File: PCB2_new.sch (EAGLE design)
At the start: 103 parts

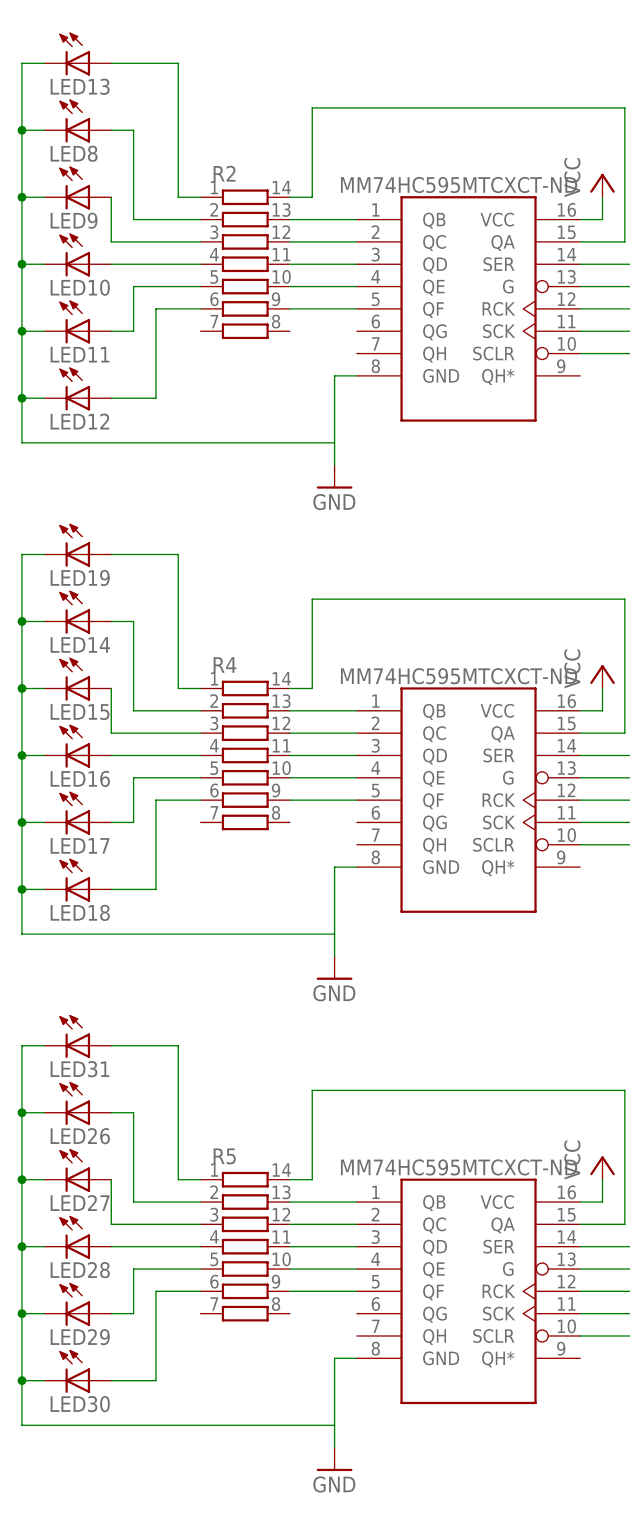
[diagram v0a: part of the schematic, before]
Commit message: Added ESD protection resistors on PCB1_new
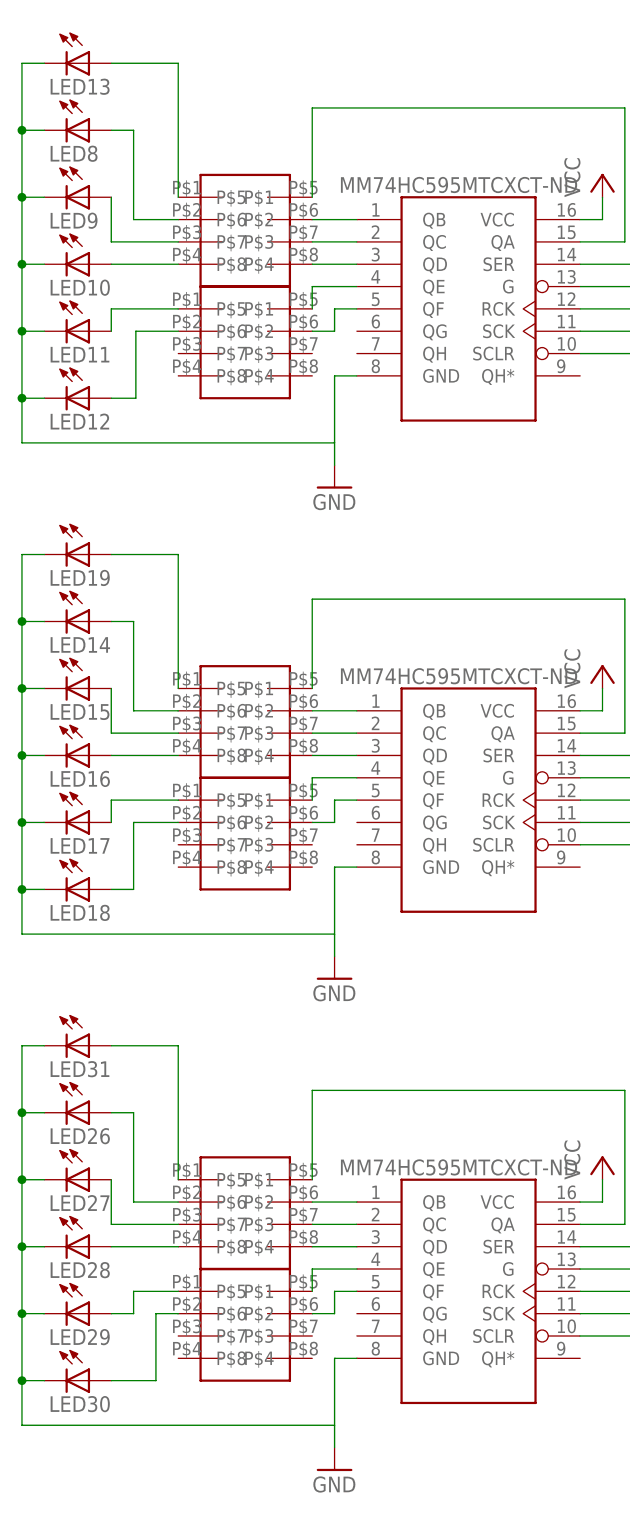
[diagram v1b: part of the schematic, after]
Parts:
- removed R2, R4, R5: (no value), resistor-bourns:4814P-T01
- added U$74, U$75, U$76, U$77, U$78, U$79: MNR04MRAPJ680, ECE477_Guitutar:MNR04MRAPJ680
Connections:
- removed net N$28: LED10.A, R2.4
- removed net N$30: LED12.A, R2.6
- removed net N$35: R4.13, U$3.QB
- removed net N$36: R4.12, U$3.QC
- removed net N$37: R4.11, U$3.QD
- removed net N$38: R4.10, U$3.QE
- removed net N$39: R4.9, U$3.QF
- removed net N$46: LED16.A, R4.4
- removed net N$47: LED17.A, R4.5
- removed net N$60: R5.13, U$5.QB
- removed net N$61: R5.12, U$5.QC
- removed net N$62: R5.11, U$5.QD
- removed net N$63: R5.10, U$5.QE
- removed net N$64: R5.9, U$5.QF
- removed net N$70: LED28.A, R5.4
- removed net N$72: LED30.A, R5.6
- new net N$10: U$3.QB, U$76.P$6
- new net N$11: U$3.QC, U$76.P$7
- new net N$12: U$3.QD, U$76.P$8
- new net N$13: U$3.QE, U$77.P$5
- new net N$15: U$3.QF, U$77.P$6
- new net N$16: LED17.A, U$77.P$1
- new net N$17: LED30.A, U$79.P$2
- new net N$18: LED28.A, U$78.P$4
- new net N$2: LED10.A, U$75.P$4
- new net N$3: LED12.A, U$74.P$2
- new net N$4: U$1.QB, U$75.P$6
- new net N$5: U$1.QC, U$75.P$7
- new net N$6: U$1.QD, U$75.P$8
- new net N$7: U$1.QE, U$74.P$5
- new net N$8: U$1.QF, U$74.P$6
- new net N$9: LED16.A, U$76.P$4
- net N$19: now also U$5.QD, U$78.P$8; no longer R2.13, U$1.QB
- net N$20: now also U$5.QC, U$78.P$7; no longer R2.12, U$1.QC
- net N$21: now also U$5.QB, U$78.P$6; no longer R2.11, U$1.QD
- net N$22: now also U$5.QE, U$79.P$5; no longer R2.10, U$1.QE
- net N$23: now also U$5.QF, U$79.P$6; no longer R2.9, U$1.QF
- net N$24: now also U$75.P$5; no longer R2.14
- net N$25: now also U$75.P$1; no longer R2.1
- net N$26: now also U$75.P$2; no longer R2.2
- net N$27: now also U$75.P$3; no longer R2.3
- net N$29: now also U$74.P$1; no longer R2.5
- net N$40: now also U$76.P$5; no longer R4.14
- net N$41: now also U$76.P$1; no longer R4.1
- net N$43: now also U$76.P$2; no longer R4.2
- net N$44: now also U$76.P$3; no longer R4.3
- net N$49: now also U$77.P$2; no longer R4.6
- net N$66: now also U$78.P$5; no longer R5.14
- net N$67: now also U$78.P$1; no longer R5.1
- net N$68: now also U$78.P$2; no longer R5.2
- net N$69: now also U$78.P$3; no longer R5.3
- net N$71: now also U$79.P$1; no longer R5.5

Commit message: PCB2 for remote work
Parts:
- added R1, R2, R3: 330k, rcl:R-US_M0805
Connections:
- new net N$31: PAD3.P, R3.1
- net FRET3: now also R1.1, R1.2
- net FRET4: now also R2.1, R2.2
- net FRET5: now also R3.2; no longer PAD3.P
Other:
- moved on the sheet: PAD3
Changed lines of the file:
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@@
 <layers>
 <layer number="1" name="Top" color="4" fill="1" visible="no" active="no"/>
+<layer number="2" name="Route2" color="1" fill="3" visible="no" active="no"/>
+<layer number="3" name="Route3" color="4" fill="3" visible="no" active="no"/>
+<layer number="4" name="Route4" color="1" fill="4" visible="no" active="no"/>
+<layer number="5" name="Route5" color="4" fill="4" visible="no" active="no"/>
+<layer number="6" name="Route6" color="1" fill="8" visible="no" active="no"/>
+<layer number="7" name="Route7" color="4" fill="8" visible="no" active="no"/>
+<layer number="8" name="Route8" color="1" fill="2" visible="no" active="no"/>
+<layer number="9" name="Route9" color="4" fill="2" visible="no" active="no"/>
+<layer number="10" name="Route10" color="1" fill="7" visible="no" active="no"/>
+<layer number="11" name="Route11" color="4" fill="7" visible="no" active="no"/>
+<layer number="12" name="Route12" color="1" fill="5" visible="no" active="no"/>
+<layer number="13" name="Route13" color="4" fill="5" visible="no" active="no"/>
+<layer number="14" name="Route14" color="1" fill="6" visible="no" active="no"/>
+<layer number="15" name="Route15" color="4" fill="6" visible="no" active="no"/>
 <layer number="16" name="Bottom" color="1" fill="1" visible="no" active="no"/>
 <layer number="17" name="Pads" color="2" fill="1" visible="no" active="no"/>
@@
 <part name="U$78" library="ECE477_Guitutar" deviceset="MNR04MRAPJ680" device=""/>
 <part name="U$79" library="ECE477_Guitutar" deviceset="MNR04MRAPJ680" device=""/>
+<part name="R1" library="rcl" deviceset="R-US_" device="M0805" value="330k"/>
+<part name="R2" library="rcl" deviceset="R-US_" device="M0805" value="330k"/>
+<part name="R3" library="rcl" deviceset="R-US_" device="M0805" value="330k"/>
 </parts>
 <sheets>
@@
 <instance part="PAD1" gate="G$1" x="144.78" y="259.08" rot="R270"/>
 <instance part="PAD2" gate="G$1" x="200.66" y="259.08" rot="R270"/>
-<instance part="PAD3" gate="G$1" x="259.08" y="259.08" rot="R270"/>
+<instance part="PAD3" gate="G$1" x="238.76" y="259.08" rot="R270"/>
 <instance part="H1" gate="G$1" x="370.84" y="248.92" rot="R270"/>
 <instance part="H2" gate="G$1" x="373.38" y="66.04" rot="R270"/>
@@
 <instance part="U$78" gate="MNR04MRAPJ680" x="48.26" y="77.47"/>
 <instance part="U$79" gate="MNR04MRAPJ680" x="48.26" y="64.77"/>
+<instance part="R1" gate="G$1" x="154.94" y="251.46"/>
+<instance part="R2" gate="G$1" x="208.28" y="251.46"/>
+<instance part="R3" gate="G$1" x="246.38" y="251.46"/>
 </instances>
 <busses>
@@
 <pinref part="PAD1" gate="G$1" pin="P"/>
 <wire x1="144.78" y1="256.54" x2="144.78" y2="251.46" width="0.1524" layer="91"/>
-<wire x1="144.78" y1="251.46" x2="152.4" y2="251.46" width="0.1524" layer="91"/>
-<label x="152.4" y="251.46" size="1.27" layer="95" xref="yes"/>
+<wire x1="144.78" y1="251.46" x2="149.86" y2="251.46" width="0.1524" layer="91"/>
+<pinref part="R1" gate="G$1" pin="1"/>
+</segment>
+<segment>
+<wire x1="160.02" y1="251.46" x2="162.56" y2="251.46" width="0.1524" layer="91"/>
+<pinref part="R1" gate="G$1" pin="2"/>
+<label x="162.56" y="251.46" size="1.27" layer="95" xref="yes"/>
 </segment>
 </net>
@@
 <pinref part="PAD2" gate="G$1" pin="P"/>
 <wire x1="200.66" y1="256.54" x2="200.66" y2="251.46" width="0.1524" layer="91"/>
-<wire x1="200.66" y1="251.46" x2="208.28" y2="251.46" width="0.1524" layer="91"/>
-<label x="208.28" y="251.46" size="1.27" layer="95" xref="yes"/>
+<wire x1="200.66" y1="251.46" x2="203.2" y2="251.46" width="0.1524" layer="91"/>
+<pinref part="R2" gate="G$1" pin="1"/>
+</segment>
+<segment>
+<wire x1="213.36" y1="251.46" x2="215.9" y2="251.46" width="0.1524" layer="91"/>
+<pinref part="R2" gate="G$1" pin="2"/>
+<label x="215.9" y="251.46" size="1.27" layer="95" xref="yes"/>
 </segment>
 </net>
@@
 </segment>
 <segment>
-<pinref part="PAD3" gate="G$1" pin="P"/>
-<wire x1="259.08" y1="256.54" x2="259.08" y2="251.46" width="0.1524" layer="91"/>
-<wire x1="259.08" y1="251.46" x2="251.46" y2="251.46" width="0.1524" layer="91"/>
-<label x="251.46" y="251.46" size="1.27" layer="95" rot="R180" xref="yes"/>
+<label x="254" y="251.46" size="1.27" layer="95" xref="yes"/>
+<wire x1="251.46" y1="251.46" x2="254" y2="251.46" width="0.1524" layer="91"/>
+<pinref part="R3" gate="G$1" pin="2"/>
 </segment>
 </net>
@@
 </segment>
 </net>
+<net name="N$31" class="0">
+<segment>
+<pinref part="PAD3" gate="G$1" pin="P"/>
+<wire x1="238.76" y1="256.54" x2="238.76" y2="251.46" width="0.1524" layer="91"/>
+<pinref part="R3" gate="G$1" pin="1"/>
+<wire x1="238.76" y1="251.46" x2="241.3" y2="251.46" width="0.1524" layer="91"/>
+</segment>
+</net>

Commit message: Finished changing dimensions for PCB3 and switched out resistors for smaller ones.
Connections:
- removed net N$14: U$71.P$1, U$71.P$2
- removed net N$48: U$70.P$1, U$70.P$2
- removed net N$51: U$72.P$1, U$72.P$2
- net RCK: now also U$72.P$1, U$72.P$2
- net SCK: now also U$70.P$1, U$70.P$2
- net SCLR: now also U$71.P$1, U$71.P$2
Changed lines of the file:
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@@
 <?xml version="1.0" encoding="utf-8"?>
 <!DOCTYPE eagle SYSTEM "eagle.dtd">
-<eagle version="8.1.0">
+<eagle version="8.0.1">
 <drawing>
 <settings>
@@
 <junction x="96.52" y="66.04"/>
 </segment>
+<segment>
+<wire x1="180.34" y1="81.28" x2="177.8" y2="81.28" width="0.1524" layer="91"/>
+<label x="177.8" y="81.28" size="1.27" layer="95" rot="R180" xref="yes"/>
+<pinref part="U$70" gate="G$1" pin="P$1"/>
+</segment>
+<segment>
+<pinref part="U$70" gate="G$1" pin="P$2"/>
+<wire x1="195.58" y1="81.28" x2="198.12" y2="81.28" width="0.1524" layer="91"/>
+<label x="198.12" y="81.28" size="1.27" layer="95" xref="yes"/>
+</segment>
 </net>
 <net name="RCK" class="0">
@@
 <junction x="99.06" y="68.58"/>
 </segment>
+<segment>
+<pinref part="U$72" gate="G$1" pin="P$2"/>
+<wire x1="195.58" y1="71.12" x2="198.12" y2="71.12" width="0.1524" layer="91"/>
+<label x="198.12" y="71.12" size="1.27" layer="95" xref="yes"/>
+</segment>
+<segment>
+<wire x1="180.34" y1="71.12" x2="177.8" y2="71.12" width="0.1524" layer="91"/>
+<label x="177.8" y="71.12" size="1.27" layer="95" rot="R180" xref="yes"/>
+<pinref part="U$72" gate="G$1" pin="P$1"/>
+</segment>
 </net>
 <net name="N$24" class="0">
@@
 <junction x="93.98" y="63.5"/>
 </segment>
+<segment>
+<wire x1="180.34" y1="76.2" x2="177.8" y2="76.2" width="0.1524" layer="91"/>
+<label x="177.8" y="76.2" size="1.27" layer="95" rot="R180" xref="yes"/>
+<pinref part="U$71" gate="G$1" pin="P$1"/>
+</segment>
+<segment>
+<pinref part="U$71" gate="G$1" pin="P$2"/>
+<wire x1="195.58" y1="76.2" x2="198.12" y2="76.2" width="0.1524" layer="91"/>
+<label x="198.12" y="76.2" size="1.27" layer="95" xref="yes"/>
+</segment>
 </net>
 <net name="LED_SER1" class="0">
@@
 </segment>
 </net>
-<net name="N$48" class="0">
-<segment>
-<pinref part="U$70" gate="G$1" pin="P$2"/>
-<wire x1="195.58" y1="81.28" x2="198.12" y2="81.28" width="0.1524" layer="91"/>
-<label x="198.12" y="81.28" size="1.27" layer="95" xref="yes"/>
-</segment>
-<segment>
-<wire x1="180.34" y1="81.28" x2="177.8" y2="81.28" width="0.1524" layer="91"/>
-<label x="177.8" y="81.28" size="1.27" layer="95" rot="R180" xref="yes"/>
-<pinref part="U$70" gate="G$1" pin="P$1"/>
-</segment>
-</net>
-<net name="N$14" class="0">
-<segment>
-<pinref part="U$71" gate="G$1" pin="P$2"/>
-<wire x1="195.58" y1="76.2" x2="198.12" y2="76.2" width="0.1524" layer="91"/>
-<label x="198.12" y="76.2" size="1.27" layer="95" xref="yes"/>
-</segment>
-<segment>
-<wire x1="180.34" y1="76.2" x2="177.8" y2="76.2" width="0.1524" layer="91"/>
-<label x="177.8" y="76.2" size="1.27" layer="95" rot="R180" xref="yes"/>
-<pinref part="U$71" gate="G$1" pin="P$1"/>
-</segment>
-</net>
-<net name="N$51" class="0">
-<segment>
-<pinref part="U$72" gate="G$1" pin="P$2"/>
-<wire x1="195.58" y1="71.12" x2="198.12" y2="71.12" width="0.1524" layer="91"/>
-<label x="198.12" y="71.12" size="1.27" layer="95" xref="yes"/>
-</segment>
-<segment>
-<wire x1="180.34" y1="71.12" x2="177.8" y2="71.12" width="0.1524" layer="91"/>
-<label x="177.8" y="71.12" size="1.27" layer="95" rot="R180" xref="yes"/>
-<pinref part="U$72" gate="G$1" pin="P$1"/>
-</segment>
-</net>

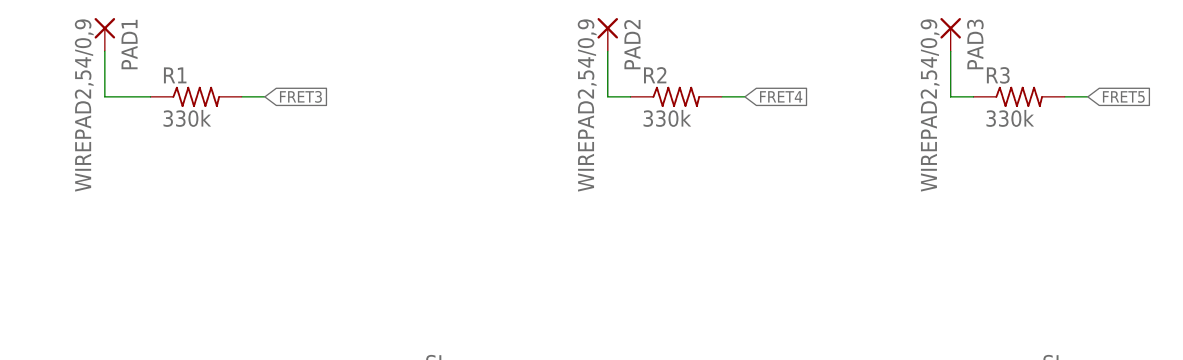
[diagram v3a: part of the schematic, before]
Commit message: Updated ref des to match those in BOM
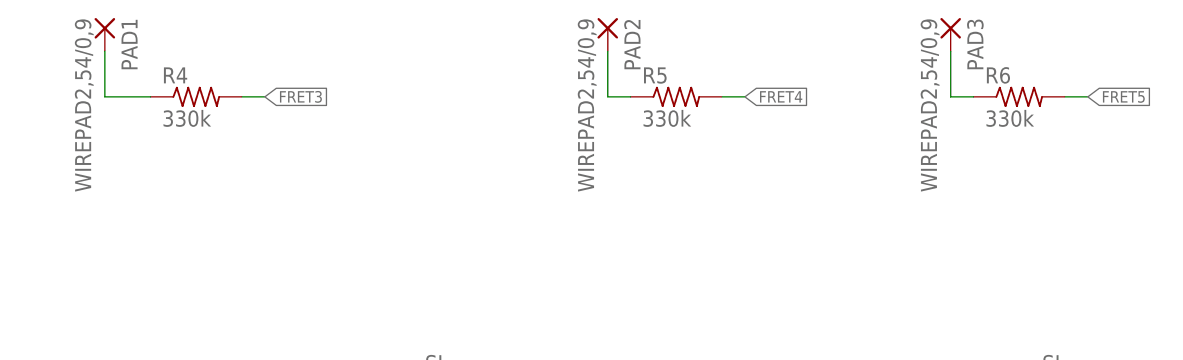
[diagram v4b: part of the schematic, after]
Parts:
- renumbered R1 to R4, R2 to R5, R3 to R6
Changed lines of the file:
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@@
 <?xml version="1.0" encoding="utf-8"?>
 <!DOCTYPE eagle SYSTEM "eagle.dtd">
-<eagle version="8.0.1">
+<eagle version="8.1.0">
 <drawing>
 <settings>
@@
 <part name="U$78" library="ECE477_Guitutar" deviceset="MNR04MRAPJ680" device=""/>
 <part name="U$79" library="ECE477_Guitutar" deviceset="MNR04MRAPJ680" device=""/>
-<part name="R1" library="rcl" deviceset="R-US_" device="M0805" value="330k"/>
-<part name="R2" library="rcl" deviceset="R-US_" device="M0805" value="330k"/>
-<part name="R3" library="rcl" deviceset="R-US_" device="M0805" value="330k"/>
+<part name="R4" library="rcl" deviceset="R-US_" device="M0805" value="330k"/>
+<part name="R5" library="rcl" deviceset="R-US_" device="M0805" value="330k"/>
+<part name="R6" library="rcl" deviceset="R-US_" device="M0805" value="330k"/>
 </parts>
 <sheets>
@@
 <instance part="U$78" gate="MNR04MRAPJ680" x="48.26" y="77.47"/>
 <instance part="U$79" gate="MNR04MRAPJ680" x="48.26" y="64.77"/>
-<instance part="R1" gate="G$1" x="154.94" y="251.46"/>
-<instance part="R2" gate="G$1" x="208.28" y="251.46"/>
-<instance part="R3" gate="G$1" x="246.38" y="251.46"/>
+<instance part="R4" gate="G$1" x="154.94" y="251.46"/>
+<instance part="R5" gate="G$1" x="208.28" y="251.46"/>
+<instance part="R6" gate="G$1" x="246.38" y="251.46"/>
 </instances>
 <busses>
@@
 <wire x1="144.78" y1="256.54" x2="144.78" y2="251.46" width="0.1524" layer="91"/>
 <wire x1="144.78" y1="251.46" x2="149.86" y2="251.46" width="0.1524" layer="91"/>
-<pinref part="R1" gate="G$1" pin="1"/>
+<pinref part="R4" gate="G$1" pin="1"/>
 </segment>
 <segment>
 <wire x1="160.02" y1="251.46" x2="162.56" y2="251.46" width="0.1524" layer="91"/>
-<pinref part="R1" gate="G$1" pin="2"/>
+<pinref part="R4" gate="G$1" pin="2"/>
 <label x="162.56" y="251.46" size="1.27" layer="95" xref="yes"/>
 </segment>
@@
 <wire x1="200.66" y1="256.54" x2="200.66" y2="251.46" width="0.1524" layer="91"/>
 <wire x1="200.66" y1="251.46" x2="203.2" y2="251.46" width="0.1524" layer="91"/>
-<pinref part="R2" gate="G$1" pin="1"/>
+<pinref part="R5" gate="G$1" pin="1"/>
 </segment>
 <segment>
 <wire x1="213.36" y1="251.46" x2="215.9" y2="251.46" width="0.1524" layer="91"/>
-<pinref part="R2" gate="G$1" pin="2"/>
+<pinref part="R5" gate="G$1" pin="2"/>
 <label x="215.9" y="251.46" size="1.27" layer="95" xref="yes"/>
 </segment>
@@
 <label x="254" y="251.46" size="1.27" layer="95" xref="yes"/>
 <wire x1="251.46" y1="251.46" x2="254" y2="251.46" width="0.1524" layer="91"/>
-<pinref part="R3" gate="G$1" pin="2"/>
+<pinref part="R6" gate="G$1" pin="2"/>
 </segment>
 </net>
@@
 <pinref part="PAD3" gate="G$1" pin="P"/>
 <wire x1="238.76" y1="256.54" x2="238.76" y2="251.46" width="0.1524" layer="91"/>
-<pinref part="R3" gate="G$1" pin="1"/>
+<pinref part="R6" gate="G$1" pin="1"/>
 <wire x1="238.76" y1="251.46" x2="241.3" y2="251.46" width="0.1524" layer="91"/>
 </segment>
